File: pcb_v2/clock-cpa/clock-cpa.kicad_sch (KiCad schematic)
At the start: 30 parts, among them J1 clock_ext, J2 control panel, J3 control panel, SW1 1HZ, SW2 1KHZ, SW3 XTAL1, SW4 XTAL2, SW5 EXT, SW6 BREAK, SW7 CLOCK_RESET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

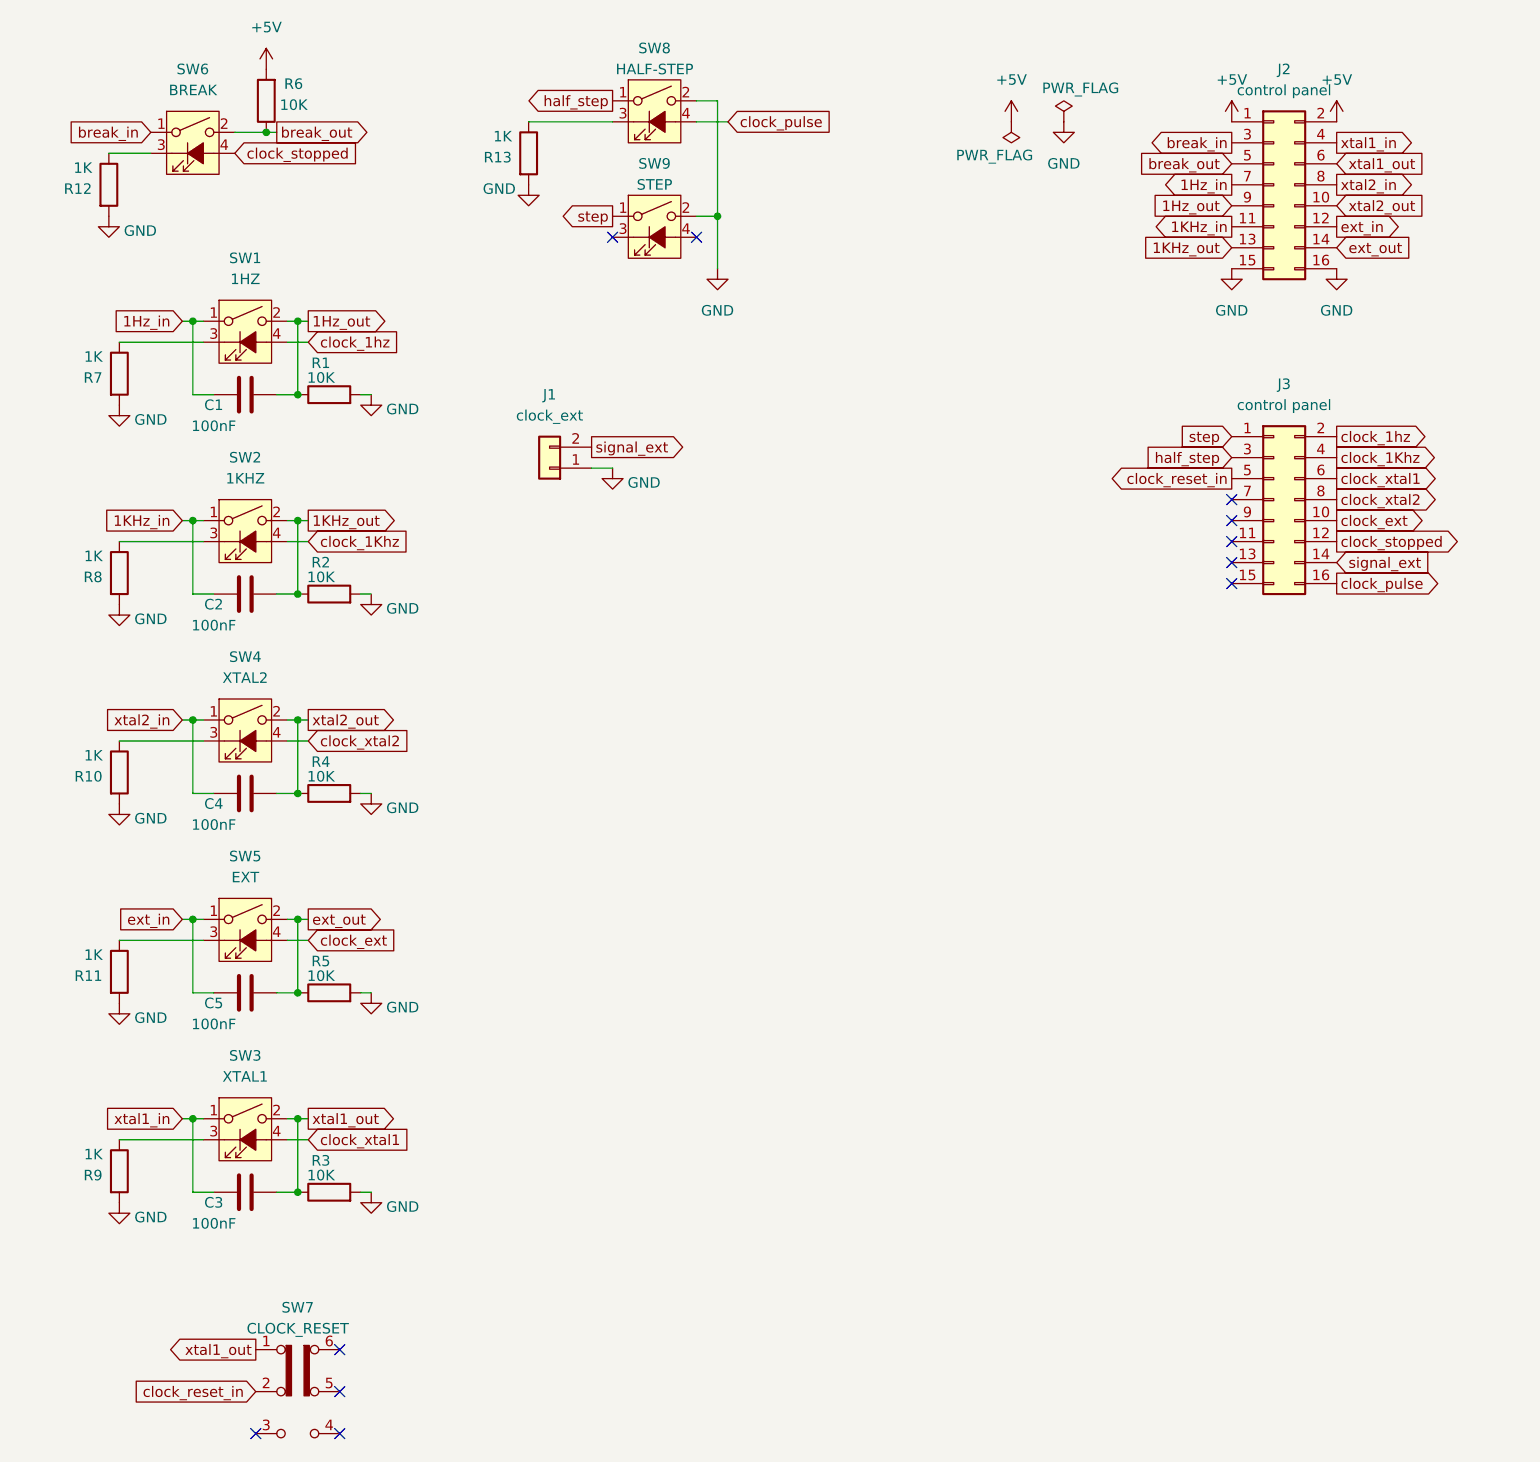
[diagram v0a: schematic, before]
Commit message: layout do painel de controle do gerador de clock
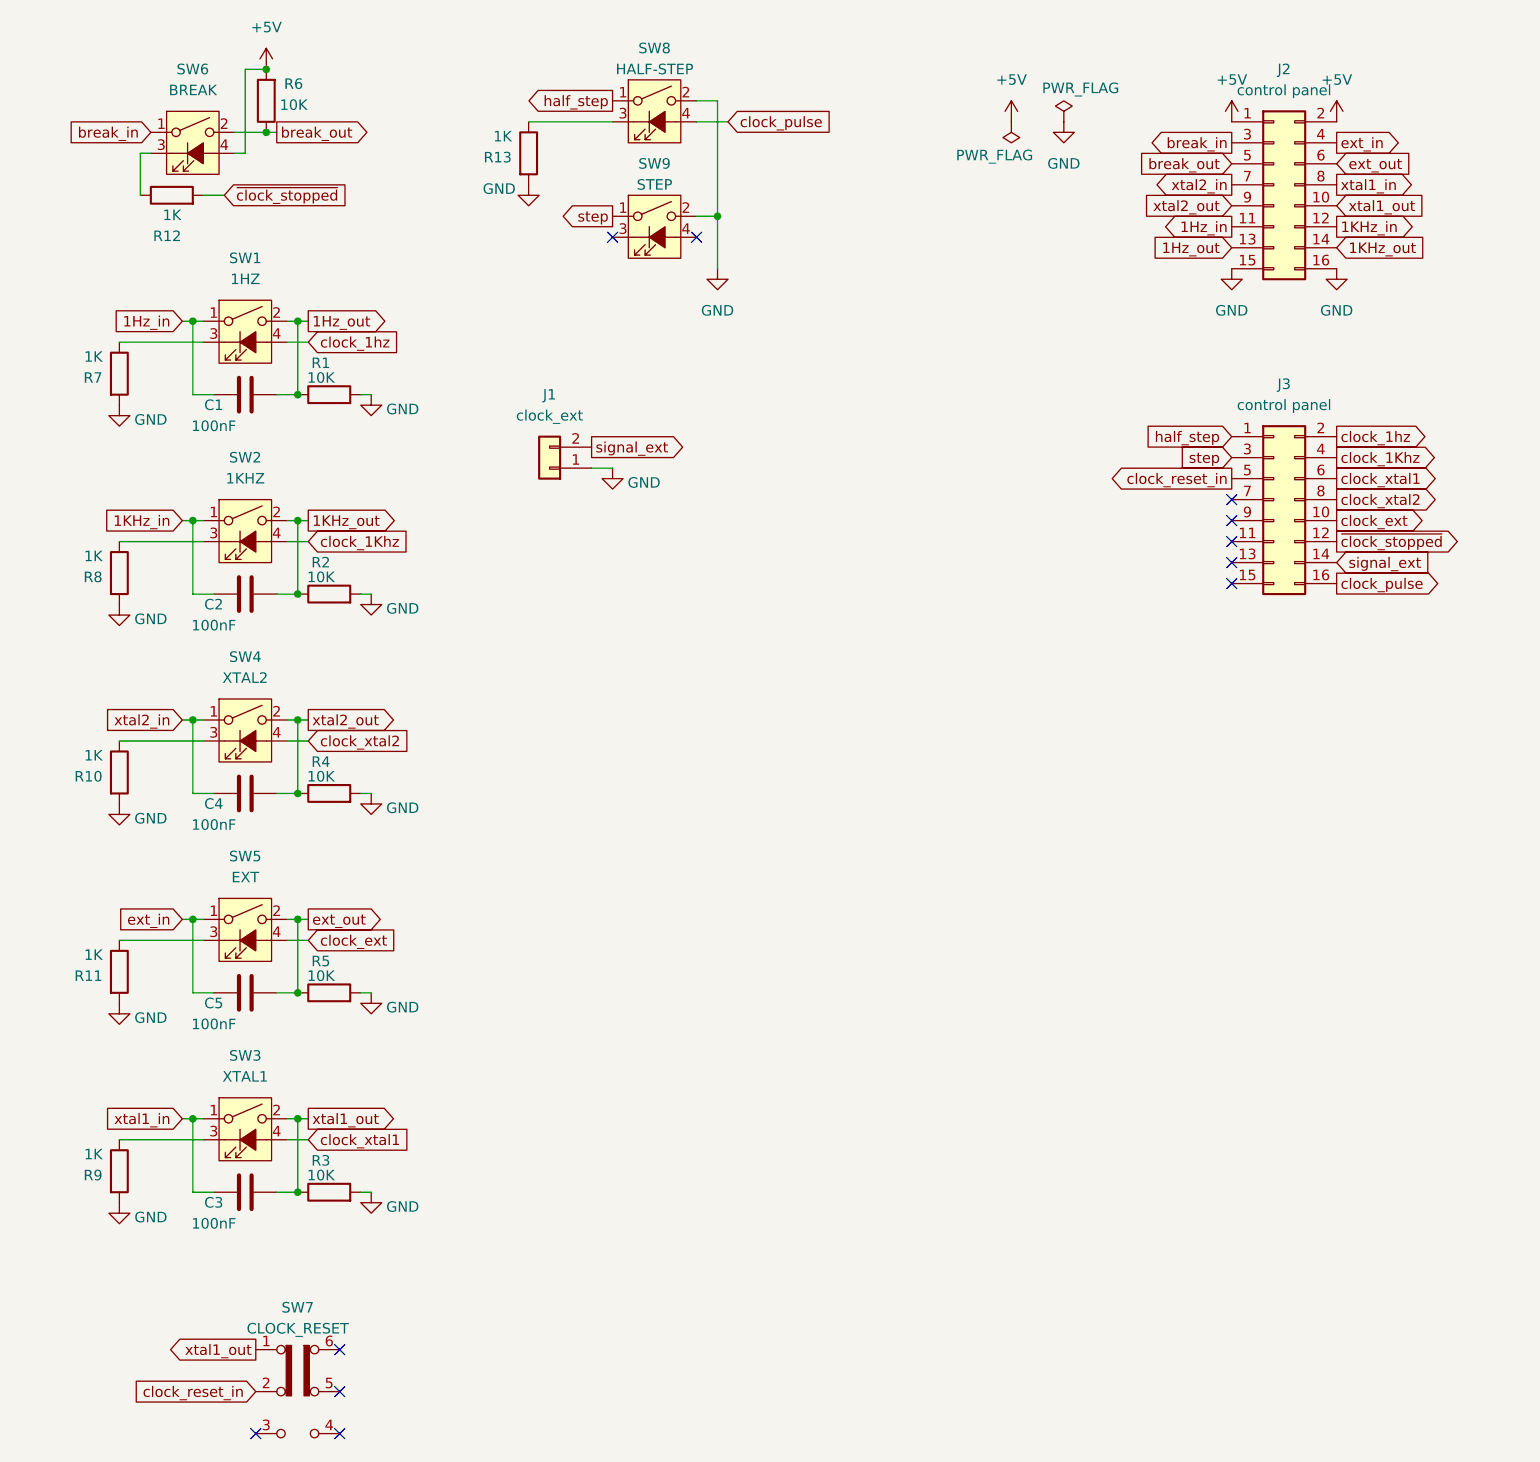
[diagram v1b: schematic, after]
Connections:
- net +5V: now also SW6.4 (A)
- net 1Hz_in: now also J2.11 (Pin_11); no longer J2.7 (Pin_7)
- net 1Hz_out: now also J2.13 (Pin_13); no longer J2.9 (Pin_9)
- net 1KHz_in: now also J2.12 (Pin_12); no longer J2.11 (Pin_11)
- net 1KHz_out: now also J2.14 (Pin_14); no longer J2.13 (Pin_13)
- net GND: no longer R12.2
- net ext_in: now also J2.4 (Pin_4); no longer J2.12 (Pin_12)
- net ext_out: now also J2.6 (Pin_6); no longer J2.14 (Pin_14)
- net half_step: now also J3.1 (Pin_1); no longer J3.3 (Pin_3)
- net step: now also J3.3 (Pin_3); no longer J3.1 (Pin_1)
- net xtal1_in: now also J2.8 (Pin_8); no longer J2.4 (Pin_4)
- net xtal1_out: now also J2.10 (Pin_10); no longer J2.6 (Pin_6)
- net xtal2_in: now also J2.7 (Pin_7); no longer J2.8 (Pin_8)
- net xtal2_out: now also J2.9 (Pin_9); no longer J2.10 (Pin_10)
- net clock_stopped renamed ~{clock_stopped}
- net ~{clock_stopped}: now also R12.2; no longer SW6.4 (A)
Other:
- moved on the sheet: R12

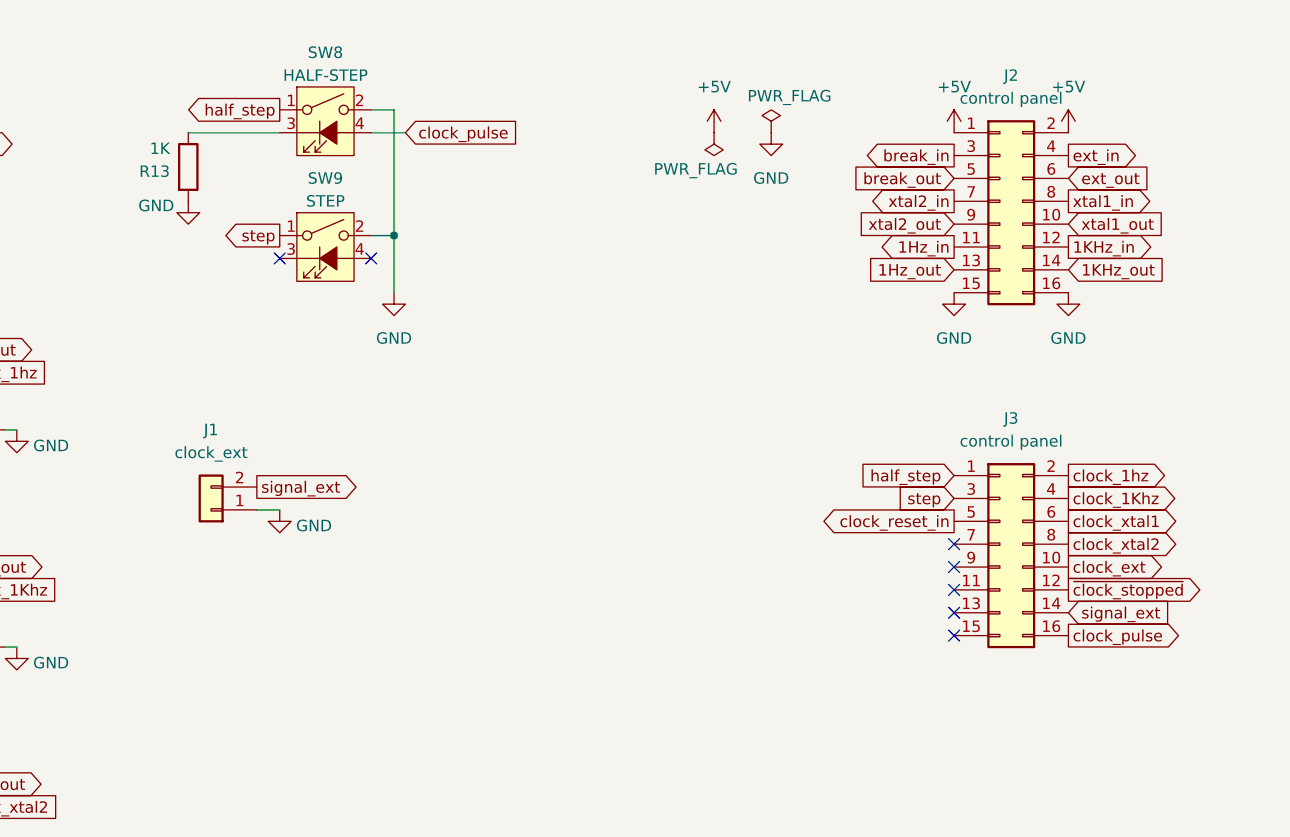
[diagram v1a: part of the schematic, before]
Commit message: Adicionado a porta para clock out; trabalhando no roteamento
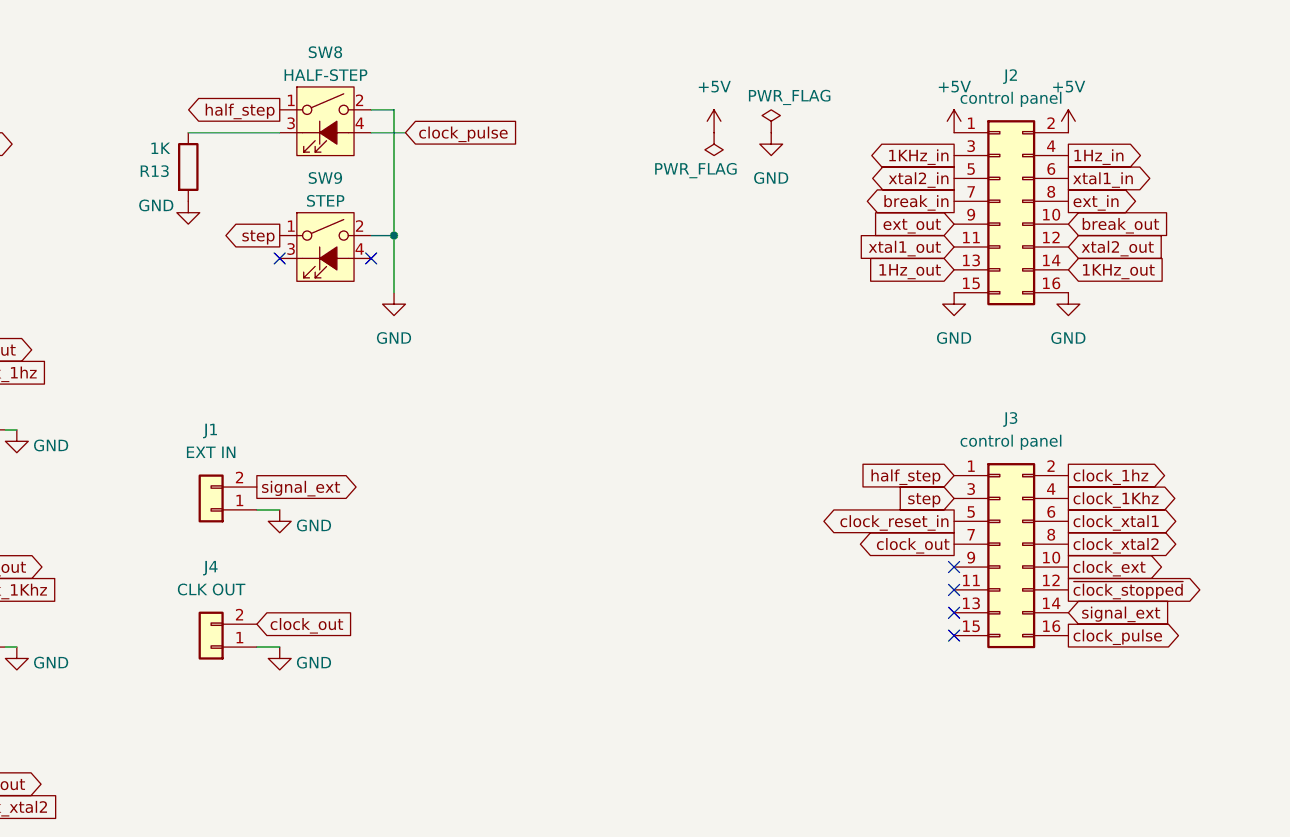
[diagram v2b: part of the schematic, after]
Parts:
- added J4: CLK OUT, Connector_Molex:Molex_KK-254_AE-6410-02A_1x02_P2.54mm_Vertical, symbol Connector_Generic:Conn_01x02
- J1: value clock_ext -> EXT IN
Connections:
- net 1Hz_in: now also J2.4 (Pin_4); no longer J2.11 (Pin_11)
- net 1KHz_in: now also J2.3 (Pin_3); no longer J2.12 (Pin_12)
- net GND: now also J4.1 (Pin_1)
- net break_in: now also J2.7 (Pin_7); no longer J2.3 (Pin_3)
- net break_out: now also J2.10 (Pin_10); no longer J2.5 (Pin_5)
- net ext_in: now also J2.8 (Pin_8); no longer J2.4 (Pin_4)
- net ext_out: now also J2.9 (Pin_9); no longer J2.6 (Pin_6)
- net xtal1_in: now also J2.6 (Pin_6); no longer J2.8 (Pin_8)
- net xtal1_out: now also J2.11 (Pin_11); no longer J2.10 (Pin_10)
- net xtal2_in: now also J2.5 (Pin_5); no longer J2.7 (Pin_7)
- net xtal2_out: now also J2.12 (Pin_12); no longer J2.9 (Pin_9)
- net clock_out: now reaches J3.7 (Pin_7)
- net clock_out: now also J4.2 (Pin_2)
- no-connect marks 11 -> 10

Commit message: layout de pcb do clock
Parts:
- added R15, R21: 10K, Resistor_THT:R_Axial_DIN0207_L6.3mm_D2.5mm_P7.62mm_Horizontal, symbol Device:R
- J1, J4: footprint Connector_Molex:Molex_KK-254_AE-6410-02A_1x02_P2.54mm_Vertical -> Connector_JST:JST_XH_B2B-XH-A_1x02_P2.50mm_Vertical
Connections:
- net +5V: now also R15.2, R21.2
- net clock_pulse: now also J3.9 (Pin_9); no longer J3.16 (Pin_16)
- net clock_reset_in: now also SW7.3 (C), SW7.4 (A); no longer SW7.2 (B)
- net half_step: now also R15.1
- net signal_ext: now also J3.11 (Pin_11); no longer J3.14 (Pin_14)
- net step: now also R21.1
- net xtal1_out: now also SW7.2 (B), SW7.5 (B); no longer SW7.1 (A)
- no-connect marks 10 -> 8
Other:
- moved on the sheet: J1, J4, R13, SW8, SW9

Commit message: continuando implementação do clock
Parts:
- removed C4: 100nF, Capacitor_THT:C_Disc_D4.7mm_W2.5mm_P5.00mm, symbol Device:C
- removed R10: 1K, Resistor_THT:R_Axial_DIN0207_L6.3mm_D2.5mm_P7.62mm_Horizontal, symbol Device:R
- removed R4: 10K, Resistor_THT:R_Axial_DIN0207_L6.3mm_D2.5mm_P7.62mm_Horizontal, symbol Device:R
- removed SW4: XTAL2, clock-buttons:TS5 LED Momentary Click Tact Switch, symbol Switch:SW_SPST_LED
- SW3: value XTAL1 -> XTAL
- SW7: footprint Button_Switch_THT:SW_CK_JS202011CQN_DPDT_Straight -> clock-buttons:Slide Switch DPDT
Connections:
- net clock_reset_in: now also SW7.1 (A), SW7.6 (C); no longer SW7.3 (C), SW7.4 (A)
- net clock_xtal2: no longer names the net of J3.8 (Pin_8)
- net xtal2_in: no longer names the net of J2.5 (Pin_5)
- net xtal2_out: no longer names the net of J2.12 (Pin_12)
- no-connect marks 8 -> 11
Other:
- moved on the sheet: C3, C5, R11, R3, R5, R9, SW3, SW5, SW7

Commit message: correções no esquemático e pcb
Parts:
- removed C1, C2, C3, C5: 100nF, Capacitor_THT:C_Disc_D4.7mm_W2.5mm_P5.00mm, symbol Device:C
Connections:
- net 1Hz_out: now also J2.14 (Pin_14); no longer J2.13 (Pin_13)
- net 1KHz_out: now also J2.13 (Pin_13); no longer J2.14 (Pin_14)
- net break_in: now also J2.8 (Pin_8); no longer J2.7 (Pin_7)
- net break_out: now also J2.9 (Pin_9); no longer J2.10 (Pin_10)
- net clock_1Khz: now also J3.3 (Pin_3); no longer J3.4 (Pin_4)
- net clock_1hz: now also J3.1 (Pin_1); no longer J3.2 (Pin_2)
- net clock_ext: now also J3.9 (Pin_9); no longer J3.10 (Pin_10)
- net clock_out: now also J3.8 (Pin_8); no longer J3.7 (Pin_7)
- net clock_pulse: now also J3.10 (Pin_10); no longer J3.9 (Pin_9)
- net clock_reset_in: now also J3.6 (Pin_6); no longer J3.5 (Pin_5)
- net clock_xtal1: now also J3.5 (Pin_5); no longer J3.6 (Pin_6)
- net ext_out: now also J2.10 (Pin_10); no longer J2.9 (Pin_9)
- net half_step: now also J3.2 (Pin_2); no longer J3.1 (Pin_1)
- net signal_ext: now also J3.12 (Pin_12); no longer J3.11 (Pin_11)
- net step: now also J3.4 (Pin_4); no longer J3.3 (Pin_3)
- net xtal1_out: now also J2.12 (Pin_12); no longer J2.11 (Pin_11)
- net ~{clock_stopped}: now also J3.11 (Pin_11); no longer J3.12 (Pin_12)
- net 1Hz_in renamed clock_stopped
- net clock_stopped: now also SW2.1, SW3.1, SW5.1
- net 1KHz_in: no longer names the net of J2.3 (Pin_3)
- net 1KHz_in: no longer SW2.1
- removed net ext_in: J2.8 (Pin_8), SW5.1
- net xtal1_in: no longer names the net of J2.6 (Pin_6)
- net xtal1_in: no longer SW3.1
- no-connect marks 11 -> 14
